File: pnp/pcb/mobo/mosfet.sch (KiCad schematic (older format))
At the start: 5 parts, among them J23 Mosfet, Q1 AO3400A

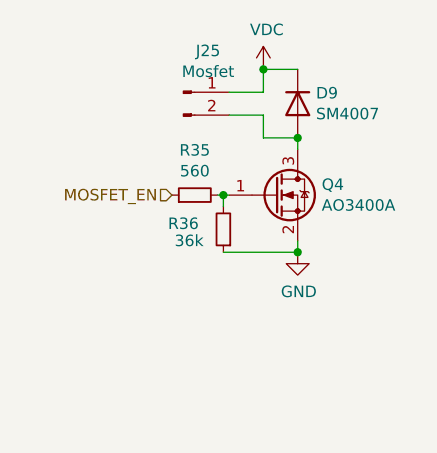
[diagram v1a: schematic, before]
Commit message: Schematic improvement proposal
Discord
@jessevdz

Fixes:
-Proper hierarchical structure
Label inside the sheets with their local name
Then connect them together at sheet-level.
- Split into functional blocks
Just like with software its good to have one function per group of components.
For example: the power input, reverse polarity protection, buckconverter, multiplexer and LDO
were connected as one block. Now they are split into their functional blocks.
- Used smaller symbols
Some symbols used their large variant, which looks a bit funny in normal schematics
For example some R's have been changed to R_Small's.
- Align symbols to grid
A lot of the symbols were off the default 50mil grid.

And a lot of other general fixes in readability and structure.
Electrically the schematic should be the same.
Improvements that would require a schematic change can possibly
be done later in a seperate commit.
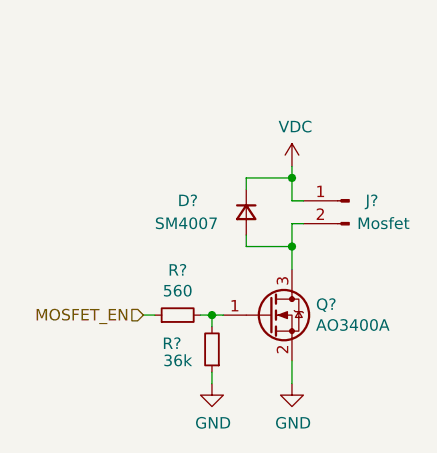
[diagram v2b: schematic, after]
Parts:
- removed D6: SM4007, Diode_SMD:D_SOD-123F, symbol Diode:SM4007
- removed J23: Mosfet, Connector_JST:JST_XH_B2B-XH-A_1x02_P2.50mm_Vertical, symbol Connector:Conn_01x02_Male
- removed Q1: AO3400A, Package_TO_SOT_SMD:SOT-23, symbol Transistor_FET:AO3400A
- removed R29: 560, Resistor_SMD:R_0805_2012Metric, symbol Device:R_Small
- removed R30: 36k, Resistor_SMD:R_0805_2012Metric, symbol Device:R_Small
- added D?: SM4007, Diode_SMD:D_SOD-123F, symbol Device:D_Small
- added J?: Mosfet, Connector_JST:JST_XH_B2B-XH-A_1x02_P2.50mm_Vertical, symbol Connector:Conn_01x02_Male
- added Q?: AO3400A, Package_TO_SOT_SMD:SOT-23, symbol Transistor_FET:AO3400A
- added R?: 560, Resistor_SMD:R_0805_2012Metric, symbol Device:R_Small
- added R?: 36k, Resistor_SMD:R_0805_2012Metric, symbol Device:R_Small
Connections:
- net GND: now also Q?.2 (S), R?.1
- net MOSFET_EN: now also R?.1
- net VDC: now also D?.1 (K), J?.1 (Pin_1)
- new net: D?.2 (A), J?.2 (Pin_2), Q?.3 (D)
- new net: Q?.1 (G), R?.2, R?.2
